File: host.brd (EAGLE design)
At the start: 82.5 x 49.3 mm, 109 parts, among them IC1 74LVC1T45GS,132, IC10 74LVC1T45GS,132, IC11 74LVC1T45GS,132, IC2 NCP187AMT120TAG, IC3 LD39200PU33R, IC4 74LVC1T45GS,132, IC5 74LVC1T45GS,132, IC6 74LVC1T45GS,132, IC7 74ALVC164245DGG:11, IC8 74ALVC164245DGG:11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

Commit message: Running through the checklist
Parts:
- added DONE: GREEN-0603, Seeed-LED:LED-0603
- added IC12: MMBT3904T, host:SOTFL50P160X78-3N
- added R29: 10K, rcl:R0201
- added R30: 100K, rcl:R0201
- moved CBSEL1 77.4 mm to (80.5, 39.5), turned to 90 degrees
- moved CBSEL0 75.0 mm to (77.0, 39.5), turned to 90 degrees
- moved R24 71.6 mm to (81.5, 45.0), turned to 90 degrees
- moved R23 68.9 mm to (78.0, 45.0), turned to 90 degrees
- moved C10 8.51 mm to (3.50, 29.0)
- moved C11 8.51 mm to (9.50, 25.0)
- moved C12 8.51 mm to (9.50, 29.0)
- moved C13 8.51 mm to (6.50, 25.0)
- moved C14 8.51 mm to (6.50, 29.0)
- moved C15 8.51 mm to (18.5, 25.0)
- moved C16 8.51 mm to (18.5, 29.0)
- moved C17 8.51 mm to (15.5, 25.0)
- moved C18 8.51 mm to (15.5, 29.0)
- moved C7 8.51 mm to (12.5, 25.0)
- moved C8 8.51 mm to (12.5, 29.0)
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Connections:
- new net N$5: IC12.1, R30.2
- new net N$6: DONE.-, IC12.3
- new net N$7: DONE.+, R29.2
- net !STATUS!: now also U$1.136
- net +3V3: now also R29.1
- net CDONE: now also R30.1
- net GND: now also IC12.2, IC7.12, IC7.37
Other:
- board text added: "!CCTL! RD5 +5V !S5! D6 D0 D1 D2 D5 D4 A0 A1 A2 A3 !S4!"
- board text added: "+5v !REF! AUDIO !MPD! !D1xx! !RESET! !EXTSEL!"
- board text added: "CLK R/!W! A10 A11 D7 D3 A12 A9 A8 A7 A6 A5 A4 GND RD4"
- board text added: "GND A15 A14 A13 !HALT! !IRQ! RSRVD"

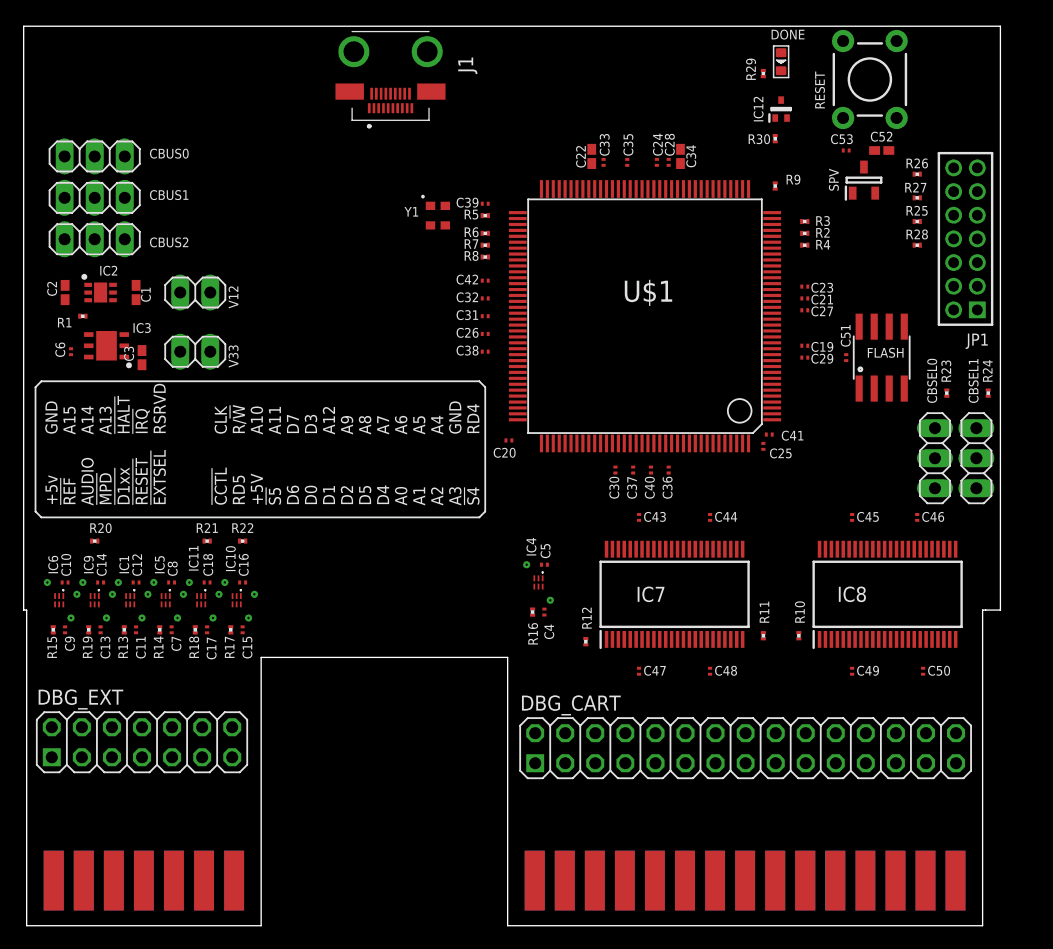
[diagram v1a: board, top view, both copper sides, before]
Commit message: Add the micro-HDMI interface
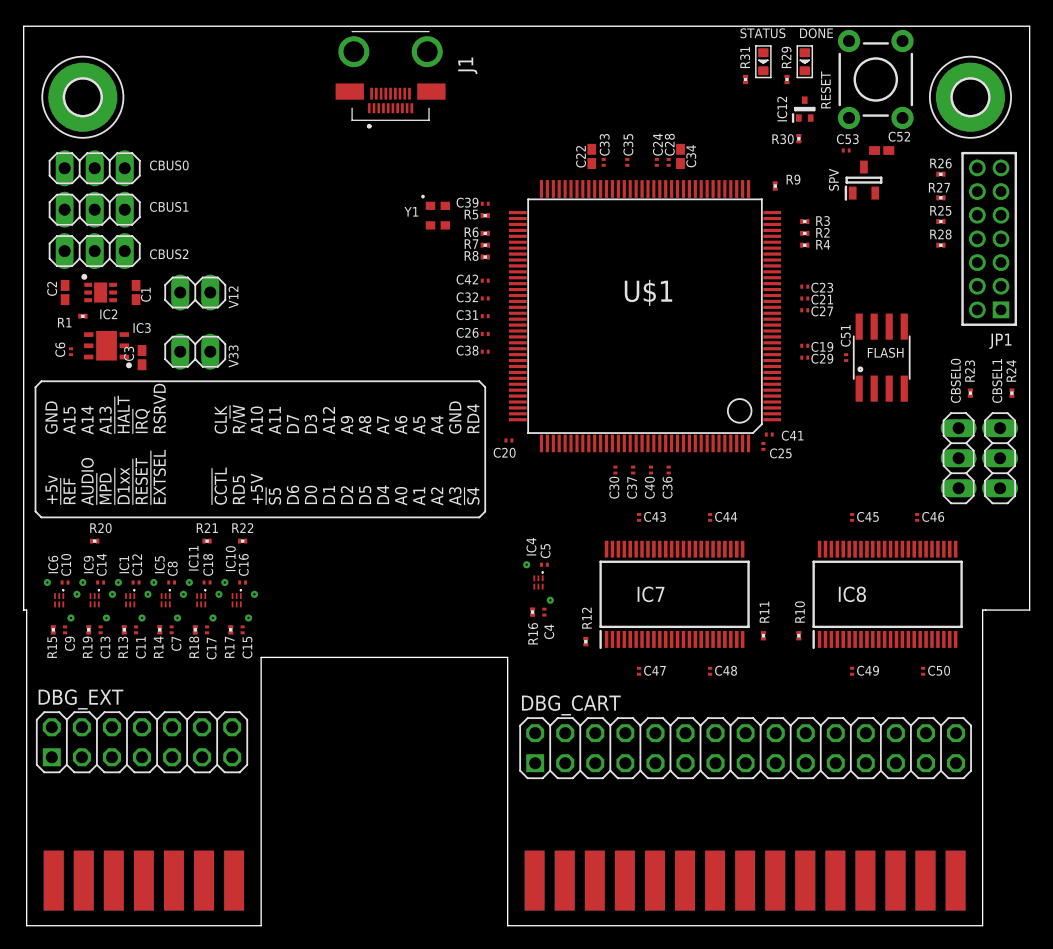
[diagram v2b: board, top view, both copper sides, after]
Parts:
- added H1, H2: MOUNT-PAD-ROUND3.0, holes:3,0-PAD
- added R31: 10K, rcl:R0201
- added STATUS: GREEN-0603, Seeed-LED:LED-0603
- moved R29 2.06 mm to (64.5, 71.5)
- moved CBSEL0 2.00 mm to (79.0, 39.5)
- moved CBSEL1 2.00 mm to (82.5, 39.5)
- moved DONE 2.00 mm to (66.0, 73.0)
- moved IC12 2.00 mm to (66.0, 69.0)
- moved JP1 2.00 mm to (81.6, 58.0)
- moved R23 2.00 mm to (80.0, 45.0)
- moved R24 2.00 mm to (83.5, 45.0)
- moved R25 2.00 mm to (77.5, 59.5)
- moved R26 2.00 mm to (77.5, 63.5)
- moved R27 2.00 mm to (77.5, 61.5)
- moved R28 2.00 mm to (77.5, 57.5)
- moved R30 2.00 mm to (65.5, 66.5)
- moved CBUS0 1.00 mm to (6.00, 64.0)
- moved CBUS1 1.00 mm to (6.00, 60.5)
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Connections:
- new net N$9: R31.2, STATUS.+
- new net XIO_BOX_CLK: J1.19, U$1.69
- new net XIO_BOX_CTS: J1.18, U$1.55
- new net XIO_BOX_RTS: J1.17, U$1.68
- new net XIO_D0: J1.3, U$1.76
- new net XIO_D1: J1.5, U$1.72
- new net XIO_D2: J1.6, U$1.83
- new net XIO_D3: J1.8, U$1.84
- new net XIO_D4: J1.9, U$1.56
- new net XIO_D5: J1.11, U$1.59
- new net XIO_D6: J1.12, U$1.66
- new net XIO_D7: J1.14, U$1.61
- new net XIO_HOST_CLK: J1.15, U$1.65
- new net XIO_HOST_CTS: J1.2, U$1.81
- new net XIO_HOST_RTS: J1.1, U$1.77
- new net XIO_SHLD1: J1.4, U$1.82
- new net XIO_SHLD2: J1.7, U$1.71
- new net XIO_SHLD3: J1.10, U$1.86
- new net XIO_SHLD4: J1.13, U$1.60
- new net XIO_SHLD5: J1.16, U$1.58
- net !STATUS!: now also STATUS.-
- net +3V3: now also R31.1
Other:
- board size 82.5 x 49.3 mm -> 85 x 49.3 mm

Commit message: Autorouted
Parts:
- added C54: 100nF, rcl:C0201
- added DBG_XIO0, DBG_XIO1: (no value), pinhead:2X05
- added LD0, LD1, LD2: GREEN-0603, Seeed-LED:LED-0603
- added R32: 12K, rcl:R0201
- added R33, R34, R35: 220R, rcl:R0201
- R29, R31: value 10K -> 220R
- moved V12 1.80 mm to (13.5, 52.0)
- moved R9 1.58 mm to (65.0, 62.0)
- moved C3 1.12 mm to (9.00, 47.5)
- moved C6 1.12 mm to (3.00, 48.0)
- moved IC3 1.12 mm to (6.00, 48.5)
- moved V33 1.12 mm to (13.5, 48.0)
- moved C1 1.00 mm to (8.50, 53.5)
- moved C2 1.00 mm to (2.50, 53.5)
- moved C41 1.00 mm to (64.0, 41.5)
- moved DONE 1.00 mm to (66.0, 72.0)
- moved IC12 1.00 mm to (66.0, 68.0)
- moved IC2 1.00 mm to (5.50, 53.5)
- moved R1 1.00 mm to (4.00, 51.5)
- moved R29 1.00 mm to (64.5, 70.5)
- moved R30 1.00 mm to (65.5, 65.5)
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- renumbered J1 to UHDMI, JP1 to TTAG
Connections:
- new net LED0: LD0.-, U$1.39
- new net LED1: LD1.-, U$1.41
- new net LED2: LD2.-, U$1.43
- new net N$13: LD0.+, R33.2
- new net N$15: LD1.+, R34.2
- new net N$16: LD2.+, R35.2
- new net N$8: R32.2, U$1.36
- net +3V3: now also C54.1, R33.1, R34.1, R35.1
- net GND: now also C54.2, DBG_XIO1.10, H1.B3,0, H2.B3,0, R32.1
- net XIO_BOX_CLK: now also DBG_XIO0.9
- net XIO_BOX_CTS: now also DBG_XIO1.9
- net XIO_BOX_RTS: now also DBG_XIO1.1
- net XIO_D0: now also DBG_XIO0.1, U$1.84; no longer U$1.76
- net XIO_D1: now also DBG_XIO0.7
- net XIO_D2: now also DBG_XIO0.6, U$1.81; no longer U$1.83
- net XIO_D3: now also DBG_XIO0.5, U$1.77; no longer U$1.84
- net XIO_D4: now also DBG_XIO1.8
- net XIO_D5: now also DBG_XIO1.6
- net XIO_D6: now also DBG_XIO1.2
- net XIO_D7: now also DBG_XIO1.4
- net XIO_HOST_CLK: now also DBG_XIO1.3
- net XIO_HOST_CTS: now also DBG_XIO0.4, U$1.83; no longer U$1.81
- net XIO_HOST_RTS: now also DBG_XIO0.2, U$1.86; no longer U$1.77
- net XIO_SHLD1: now also DBG_XIO0.3
- net XIO_SHLD2: now also DBG_XIO0.10
- net XIO_SHLD3: now also DBG_XIO0.8, U$1.76; no longer U$1.86
- net XIO_SHLD4: now also DBG_XIO1.5
- net XIO_SHLD5: now also DBG_XIO1.7
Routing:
- net GND: track 0.00 -> 470.0 mm, vias 7 -> 43
- net +3V3: track 0.00 -> 213.0 mm, vias 6 -> 39
- net +5V: track 0.00 -> 166.2 mm, vias 7 -> 15
- net A8_A14: track 0.00 -> 110.2 mm, vias 0 -> 2
- net +1.2V: track 0.00 -> 104.8 mm, vias 0 -> 13
- net XIO_D2: track 0.00 -> 89.1 mm
- net A8_A15: track 0.00 -> 85.8 mm, vias 0 -> 1
- net A8_A13: track 0.00 -> 84.3 mm, vias 0 -> 1
- net DIR_MPD: track 0.00 -> 61.7 mm, vias 0 -> 4
- net !REF!: track 0.00 -> 61.3 mm, vias 0 -> 2
- net A8_A10: track 0.00 -> 59.0 mm, vias 0 -> 1
- net DIR_REF: track 0.00 -> 56.9 mm, vias 0 -> 2
- net A8_A11: track 0.00 -> 55.9 mm, vias 0 -> 2
- net SPI_D0: track 0.00 -> 55.7 mm
- net !A8_D1XX!: track 0.00 -> 53.1 mm, vias 0 -> 1
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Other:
- board text added: "+"
- board text added: "-"
- board text added: "BOX_RTS HOST_CLK SHLD4 SHLD5 BOX_CTS"
- board text added: "D0 SHLD1 D3 D1 BOX_CLK"
- board text added: "D6 D7 D5 D4 GND"
- board text added: "H"
- board text added: "HOST_RTS HOST_CTS D2 SHLD3 SHLD2"
- board text added: "XE HOST"
- board text added: "v1 ©SjG 2021"

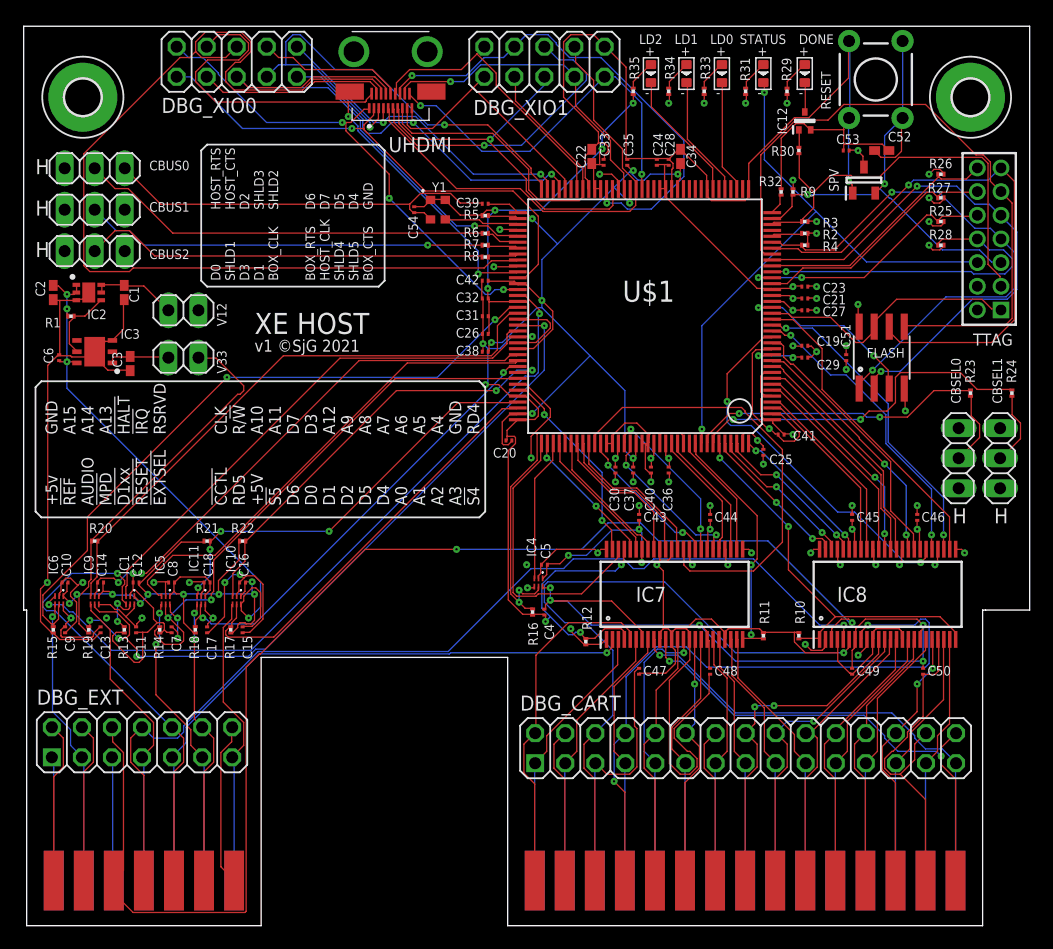
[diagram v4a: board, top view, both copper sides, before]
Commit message: Change to available parts
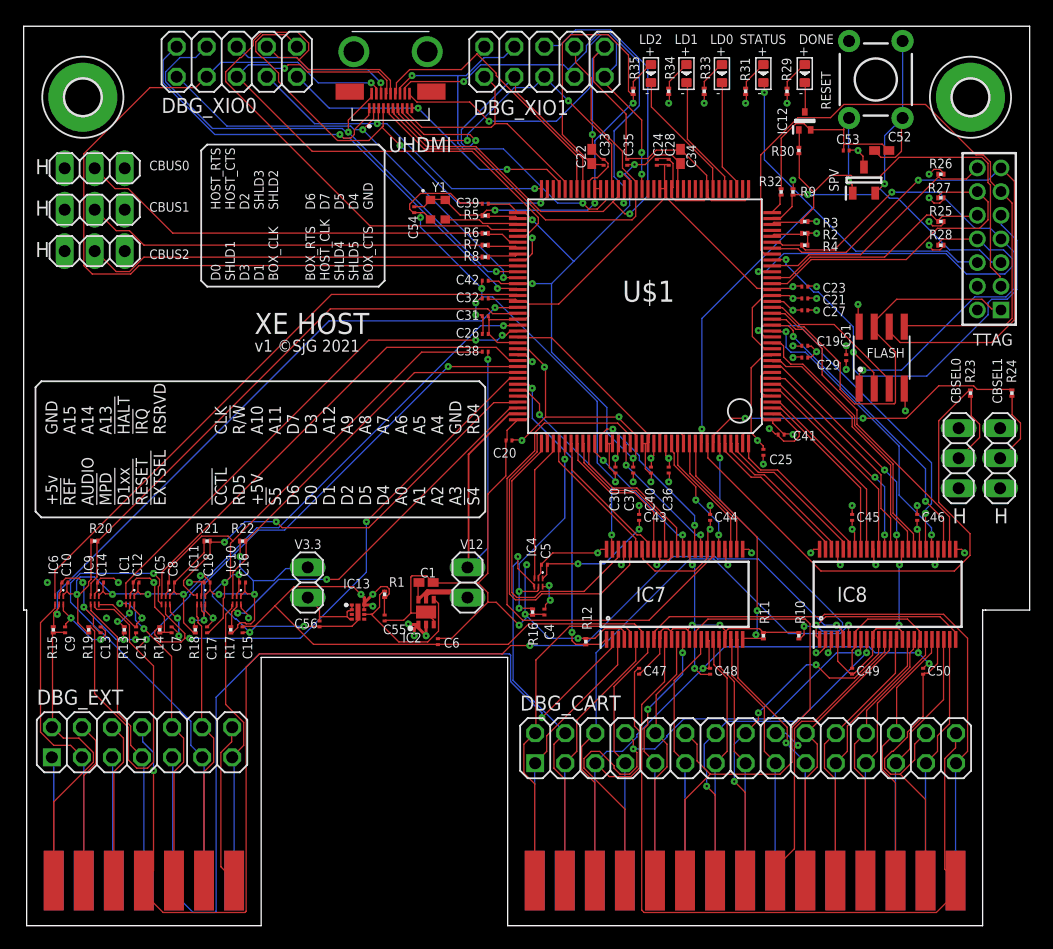
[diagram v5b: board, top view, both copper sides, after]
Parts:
- removed C2, C3: 10uF, rcl:C0402K
- removed IC3: LD39200PU33R, x-pi:SON95P300X300X100-7N
- removed V33: (no value), pinhead:1X02
- added C55, C56: 1uF, rcl:C0201
- added IC13: NCP186BMX330TAG, host:NCP186AMX330TAG
- added V3.3: (no value), pinhead:1X02
- IC12: value MMBT3904T -> MUN2211T3G
- moved C6 40.0 mm to (35.0, 24.0)
- moved IC2 39.3 mm to (34.0, 26.5), turned to 90 degrees
- moved R1 35.4 mm to (30.5, 28.0), turned to 270 degrees
- moved C1 35.4 mm to (34.0, 29.0), turned to 0 degrees
- moved V12 33.2 mm to (37.5, 29.0), turned to 270 degrees
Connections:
- removed net N$4: C3.1, IC3.1, IC3.2, V33.2
- new net N$18: C56.1, IC13.1, IC13.2, IC13.4, V3.3.2
- net +3V3: now also V3.3.1; no longer V33.1
- net +5V: now also C55.1, IC13.7, IC13.8; no longer C2.1, IC3.6
- net GND: now also C55.2, C56.2, IC13.9; no longer C2.2, C3.2, IC3.3, IC3.7
- net PWRGD_1V2: now also IC13.6; no longer IC3.5
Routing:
- net XIO_D2: track 89.1 -> 35.6 mm, vias 0 -> 2
- net D1: track 13.4 -> 45.8 mm, vias 2 -> 0
- net A8_A14: track 110.2 -> 78.6 mm, vias 2 -> 1
- net +1.2V: track 104.8 -> 132.4 mm, vias 13 -> 14
- net XIO_SHLD1: track 48.9 -> 76.0 mm
- net D6: track 37.8 -> 12.3 mm, vias 0 -> 2
- net A8_RD4: track 41.9 -> 65.3 mm, vias 2 -> 0
- net A8_D3: track 21.8 -> 44.8 mm, vias 1 -> 0
- net !A8_D1XX!: track 53.1 -> 75.9 mm
- net GND: track 470.0 -> 450.4 mm, vias 43 -> 54
- net CBSEL0: track 24.7 -> 44.2 mm, vias 2 -> 0
- net A8_A13: track 84.3 -> 102.4 mm, vias 1 -> 3
- net CLK: track 12.0 -> 29.1 mm, vias 2 -> 0
- net !A8_RESET!: track 25.3 -> 40.2 mm, vias 2 -> 1
- net XIO_D1: track 43.2 -> 28.5 mm
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
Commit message: Using only 4 layers
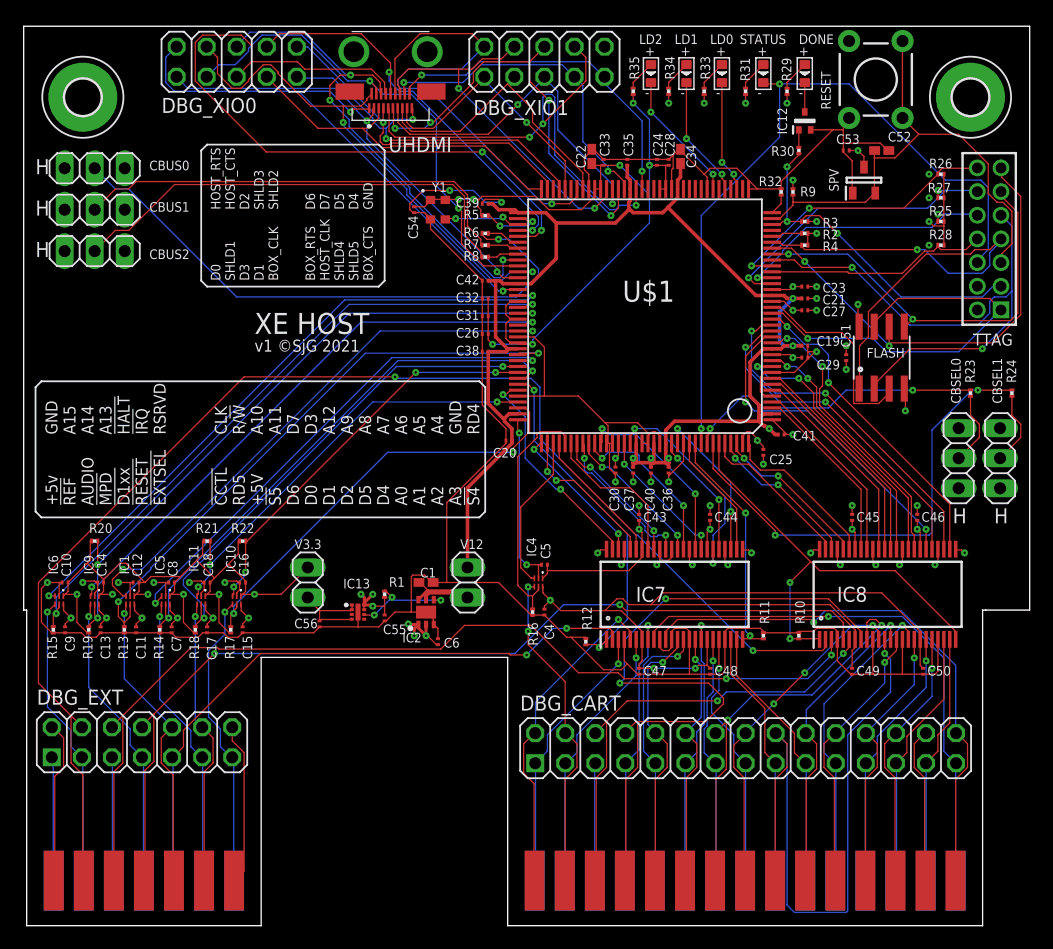
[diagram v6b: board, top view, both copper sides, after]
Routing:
- net GND: track 450.4 -> 346.5 mm, vias 54 -> 38
- net +5V: track 163.7 -> 122.6 mm, vias 19 -> 15
- net +3V3: track 223.8 -> 184.0 mm, vias 35 -> 36
- net XIO_SHLD1: track 76.0 -> 42.2 mm, vias 1 -> 2
- net A8_A15: track 81.5 -> 114.8 mm, vias 1 -> 2
- net A8_A8: track 27.5 -> 58.3 mm
- net D1: track 45.8 -> 18.6 mm, vias 0 -> 2
- net A8_D3: track 44.8 -> 22.0 mm, vias 0 -> 1
- net DIR_MPD: track 75.1 -> 52.4 mm
- net A8_A13: track 102.4 -> 80.1 mm, vias 3 -> 2
- net !A8_D1XX!: track 75.9 -> 53.9 mm, vias 1 -> 2
- net SPI_D0: track 55.7 -> 35.3 mm, vias 0 -> 2
- net XIO_SHLD3: track 54.2 -> 35.4 mm, vias 0 -> 2
- net CBSEL0: track 44.2 -> 25.5 mm, vias 0 -> 2
- net A8_RD4: track 65.3 -> 47.1 mm, vias 0 -> 1
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- removed copper zone on layer 3, net +1.2V
